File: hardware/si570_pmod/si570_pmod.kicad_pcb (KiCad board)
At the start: 2 copper layers, 40 x 20 mm, 15 parts, among them J1 Conn_01x06_Top_Bottom, J2 Conn_Coaxial, J3 Conn_Coaxial, U1 Si570

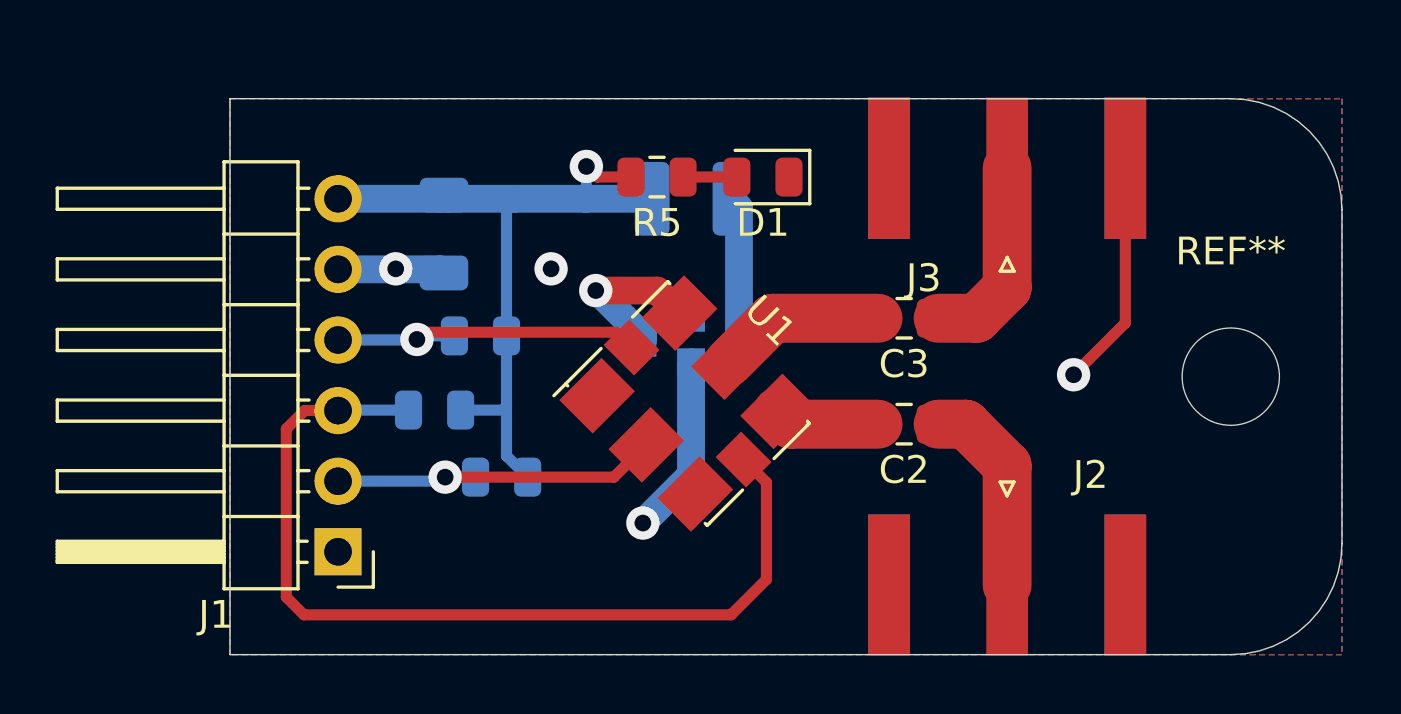
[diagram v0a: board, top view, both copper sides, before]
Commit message: fine-tune PCBs and FP, ordered first hardware
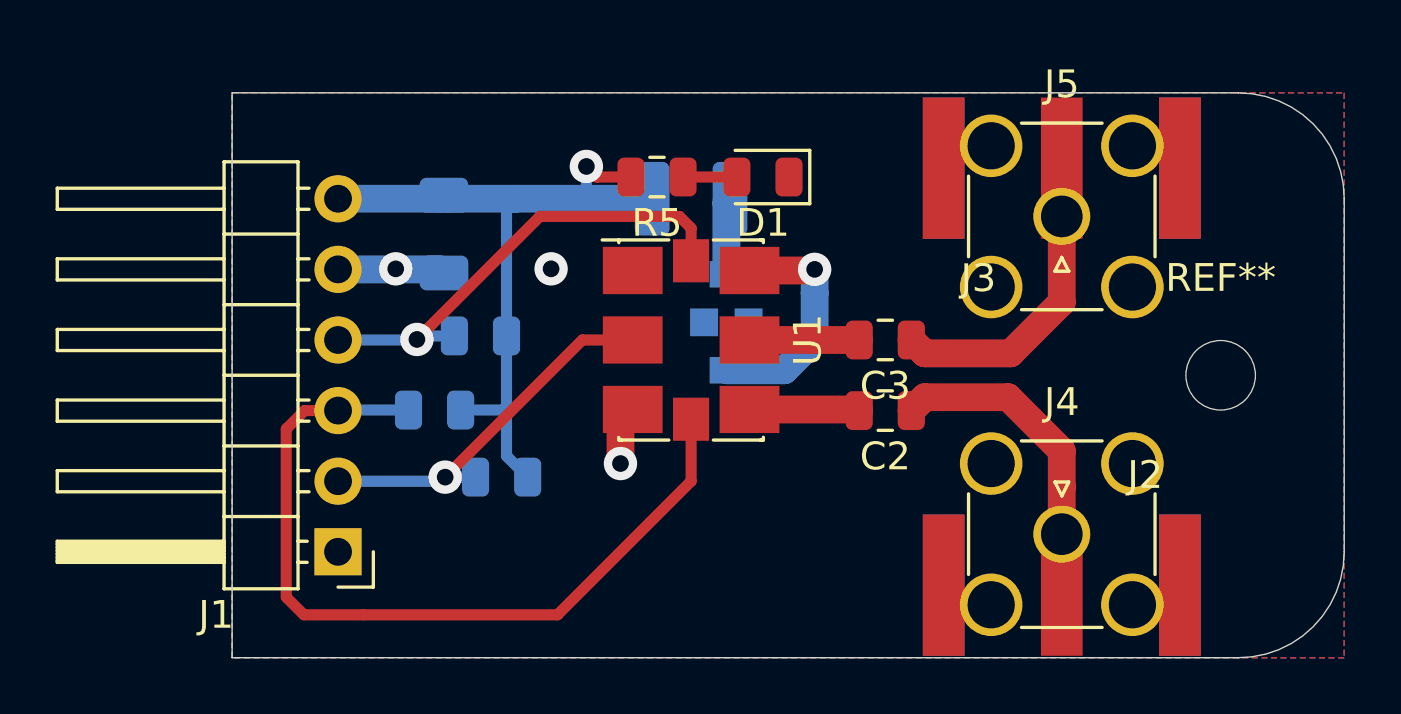
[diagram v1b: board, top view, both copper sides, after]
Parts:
- removed the REF** at (107.0, 91.0)
- added J4: Conn_Coaxial, Connector_Coaxial:SMA_Amphenol_132134-11_Vertical, F.Cu at (100.9, 96.7)
- added J5: Conn_Coaxial, Connector_Coaxial:SMA_Amphenol_132134-11_Vertical, F.Cu at (100.9, 85.2)
- added REF**: MountingHole_2.5mm, MountingHole:MountingHole_2.5mm, F.Cu at (106.6, 91.0)
- moved U1 2.29 mm to (87.6, 89.7), turned to -90 degrees
- moved J2 1.97 mm to (100.9, 98.5)
- moved J3 1.97 mm to (100.9, 83.5)
- moved C9 1.42 mm to (88.9, 89.0), turned to -90 degrees
- moved C3 1.03 mm to (94.6, 89.7)
- moved C2 0.84 mm to (94.6, 92.2)
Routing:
- net GND: track 19.4 -> 6.87 mm, vias 4 -> 3
- net /SDA: track 12.3 -> 17.7 mm
- net Net-(C3-Pad1): track 7.24 -> 11.2 mm
- net Net-(C2-Pad1): track 7.40 -> 11.2 mm
- net /SCL: track 33.4 -> 29.8 mm
- net Net-(C9-Pad3): track 5.87 -> 8.53 mm
- net Net-(C9-Pad1): track 5.21 -> 2.77 mm
- net Net-(C3-Pad2): track 6.02 -> 3.95 mm
- net /OE: track 12.8 -> 13.9 mm
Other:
- board size 40 x 20 mm -> 40 x 20.3 mm

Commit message: si570_pmod: make SMA footprint milling compatible
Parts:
- moved C2 1.27 mm to (93.3, 92.2)
- moved C3 1.27 mm to (93.3, 89.7)
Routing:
- net Net-(C2-Pad1): track 11.2 -> 22.3 mm, vias 0 -> 1
- net Net-(C3-Pad1): track 11.2 -> 22.1 mm, vias 0 -> 1
- net Net-(C3-Pad2): track 3.95 -> 2.68 mm
- net Net-(C2-Pad2): track 3.96 -> 2.69 mm
